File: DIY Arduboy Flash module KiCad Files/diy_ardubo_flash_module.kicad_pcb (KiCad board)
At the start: 2 copper layers, 71 x 86.5 mm, 27 parts, among them J2 Conn_01x07_Pin, J4 Conn_01x06_Pin, J5 Conn_01x01_Pin, Q1 BC557, SW3 SW_Push, SW4 SW_Push, SW8 SW_SPDT, U1 ProMicro

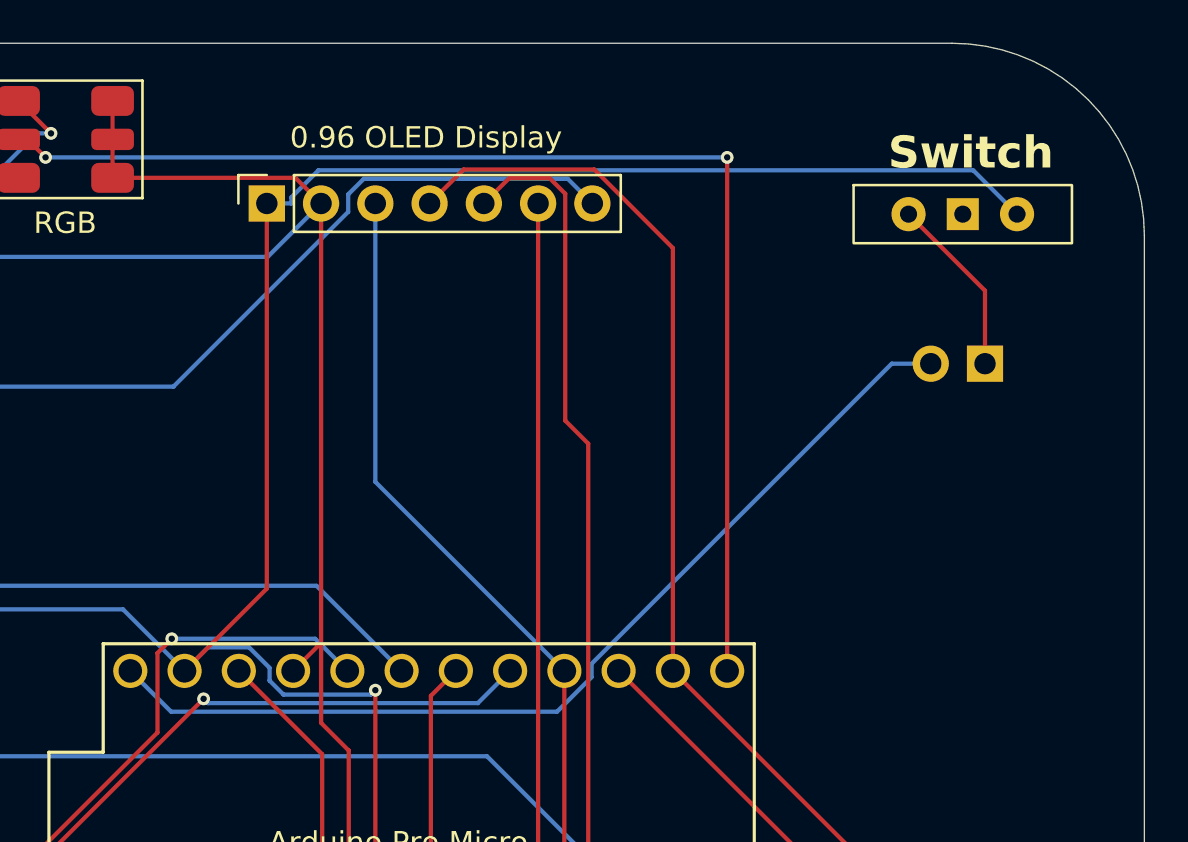
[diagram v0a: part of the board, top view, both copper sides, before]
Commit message: Updated Schematics
Fixed ground pin issue with switch
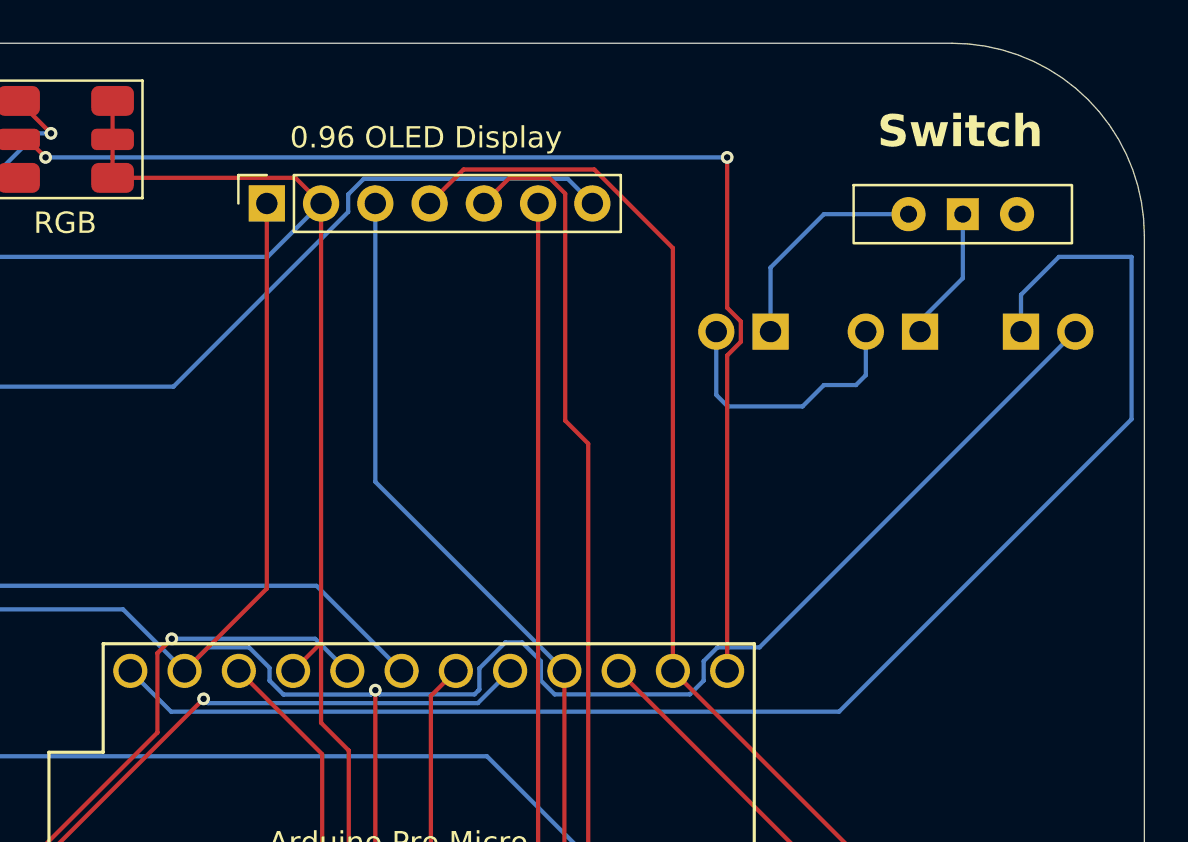
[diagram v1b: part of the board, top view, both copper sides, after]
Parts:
- removed Batt. Connector: Conn_02x01, Connector_PinHeader_2.54mm:PinHeader_2x01_P2.54mm_Vertical
- added BOOSTER IN: Conn_01x02_Pin, Connector_PinHeader_2.54mm:PinHeader_1x02_P2.54mm_Vertical, B.Cu at (167.0, 55.0)
- added BOOSTER OUT: Conn_01x02_Pin, Connector_PinHeader_2.54mm:PinHeader_1x02_P2.54mm_Vertical, B.Cu at (178.7, 55.0)
- added TP4056 OUT: Conn_01x02_Pin, Connector_PinHeader_2.54mm:PinHeader_1x02_P2.54mm_Vertical, B.Cu at (174.0, 55.0)
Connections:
- SW8 pad 1: unconnected-(SW8-A-Pad1) -> Net-(J1-Pin_1)
- SW8 pad 3: Net-(J2-GND) -> unconnected-(SW8-C-Pad3)
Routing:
- net Net-(J7-Pin_1): track 45.4 -> 68.6 mm
- net Net-(J1-Pin_2): track 0.00 -> 12.8 mm
- net Net-(J2-GND): track 110.3 -> 117.0 mm
- net Net-(J1-Pin_1): track 0.00 -> 6.33 mm
- net Net-(J6-Pin_1): track 8.48 -> 10.5 mm
- net Net-(D1-KR): track 57.6 -> 58.1 mm
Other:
- board text added: "+"
- board text added: "-"
